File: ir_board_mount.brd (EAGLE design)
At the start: 40 x 51 mm, 15 parts

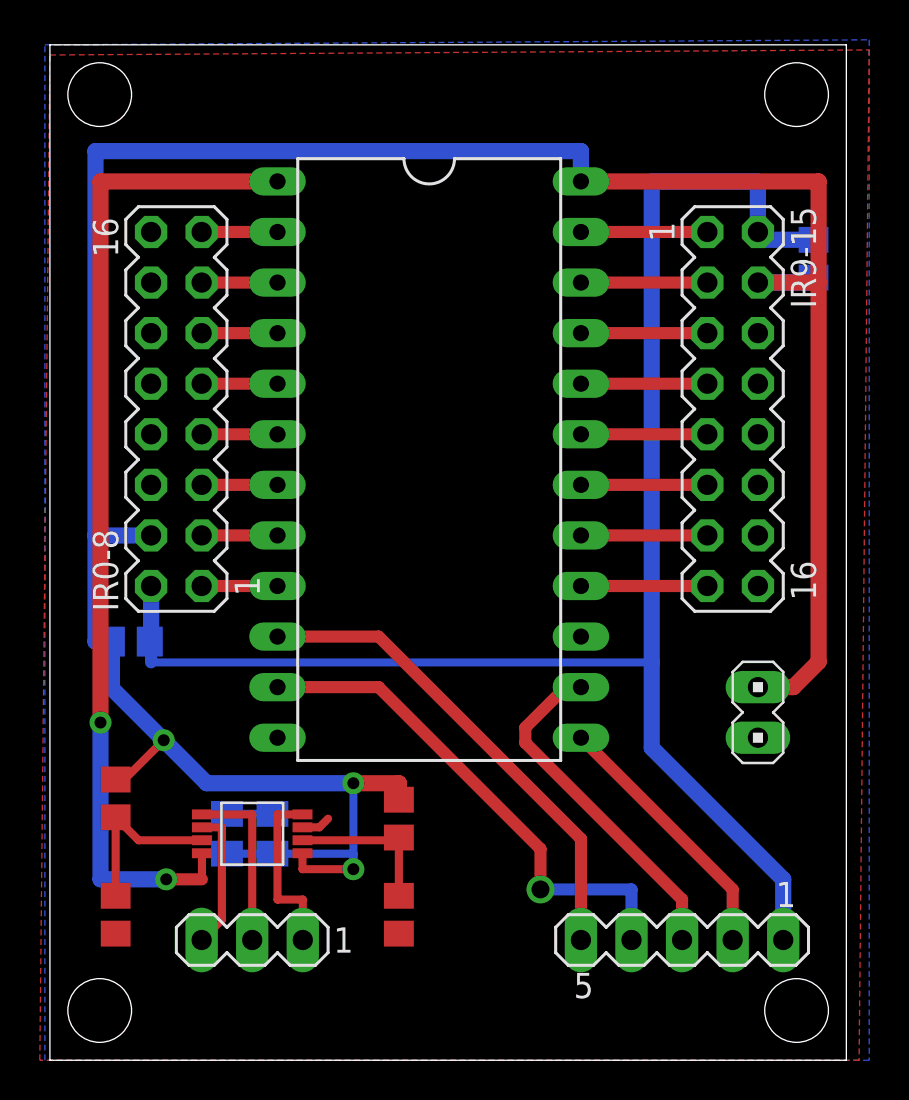
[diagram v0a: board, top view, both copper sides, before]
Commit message: Changed mount holes to vias
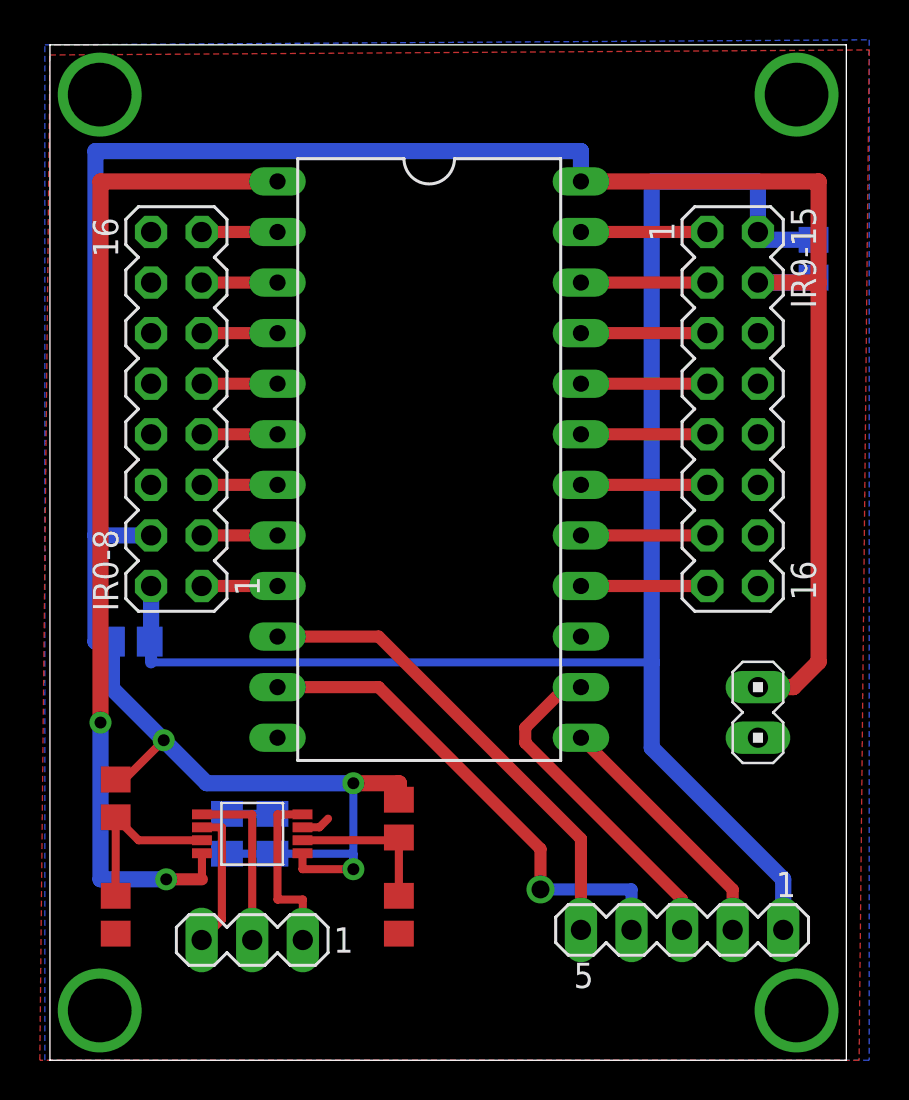
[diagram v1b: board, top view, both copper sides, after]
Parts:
- moved SV5 0.51 mm to (31.8, 3.05)
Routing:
- net N$18: track 17.6 -> 17.1 mm
- net N$17: track 13.3 -> 12.8 mm
- net A: track 24.5 -> 24.0 mm
- net LEDON: track 80.9 -> 80.4 mm
- net B: track 25.7 -> 25.2 mm
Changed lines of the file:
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@@
 v. 2013/11/27</text>
 <text x="14.224" y="9.906" size="0.8128" layer="52" rot="MR0">Debounce Caps</text>
-<hole x="2.5" y="45" drill="3.2"/>
-<hole x="37.5" y="45" drill="3.2"/>
-<hole x="37.5" y="-1" drill="3.2"/>
-<hole x="2.5" y="-1" drill="3.2"/>
 </plain>
 <attributes>
@@
 <attribute name="VALUE" x="18.161" y="38.735" size="1.778" layer="27" ratio="10" rot="R270"/>
 </element>
-<element name="SV5" library="con-lstb" package="MA05-1" value="" x="31.75" y="2.54" smashed="yes" rot="R180">
-<attribute name="OC_NEWARK" value="unknown" x="11.43" y="46.99" size="1.778" layer="27" rot="R180" display="off"/>
-<attribute name="MPN" value="" x="11.43" y="46.99" size="1.778" layer="27" rot="R180" display="off"/>
-<attribute name="MF" value="" x="11.43" y="46.99" size="1.778" layer="27" rot="R180" display="off"/>
-<attribute name="OC_FARNELL" value="unknown" x="11.43" y="46.99" size="1.778" layer="27" rot="R180" display="off"/>
-<attribute name="VALUE" x="34.29" y="5.461" size="1.27" layer="27" ratio="10" rot="R180"/>
+<element name="SV5" library="con-lstb" package="MA05-1" value="" x="31.75" y="3.048" smashed="yes" rot="R180">
+<attribute name="OC_NEWARK" value="unknown" x="11.43" y="47.498" size="1.778" layer="27" rot="R180" display="off"/>
+<attribute name="MPN" value="" x="11.43" y="47.498" size="1.778" layer="27" rot="R180" display="off"/>
+<attribute name="MF" value="" x="11.43" y="47.498" size="1.778" layer="27" rot="R180" display="off"/>
+<attribute name="OC_FARNELL" value="unknown" x="11.43" y="47.498" size="1.778" layer="27" rot="R180" display="off"/>
+<attribute name="VALUE" x="34.29" y="5.969" size="1.27" layer="27" ratio="10" rot="R180"/>
 </element>
 <element name="U$3" library="IEEE_bot_specific_parts" package="TSSOP-8" value="ADC081C021" x="10.16" y="7.874" smashed="yes" rot="R270">
@@
 <contactref element="IR9-15" pad="14"/>
 <contactref element="IR9-15" pad="16"/>
-<polygon width="0.4064" layer="1" isolate="0.254">
+<polygon width="0.4064" layer="1" isolate="0.3048">
 <vertex x="0" y="46.99"/>
 <vertex x="41.148" y="47.244"/>
@@
 <vertex x="-0.508" y="-3.5"/>
 </polygon>
-<polygon width="0.4064" layer="16" isolate="0.254">
+<polygon width="0.4064" layer="16" isolate="0.3048">
 <vertex x="-0.254" y="47.498"/>
 <vertex x="41.148" y="47.752"/>
@@
 <wire x1="5.014" y1="17.526" x2="5.08" y2="17.526" width="0.8128" layer="16"/>
 <wire x1="5.08" y1="17.526" x2="5.08" y2="20.32" width="0.8128" layer="16"/>
-<wire x1="36.83" y1="2.54" x2="36.83" y2="5.588" width="0.8128" layer="16"/>
+<wire x1="36.83" y1="3.048" x2="36.83" y2="5.588" width="0.8128" layer="16"/>
 <wire x1="36.83" y1="5.588" x2="30.226" y2="12.192" width="0.8128" layer="16"/>
 <wire x1="30.226" y1="12.192" x2="30.226" y2="16.4846" width="0.8128" layer="16"/>
@@
 <contactref element="U$2" pad="13"/>
 <contactref element="SV5" pad="2"/>
-<wire x1="34.29" y1="2.54" x2="34.29" y2="5.08" width="0.6096" layer="1"/>
+<wire x1="34.29" y1="3.048" x2="34.29" y2="5.08" width="0.6096" layer="1"/>
 <wire x1="34.29" y1="5.08" x2="26.67" y2="12.7" width="0.6096" layer="1"/>
 </signal>
@@
 <contactref element="SV5" pad="3"/>
 <contactref element="U$2" pad="14"/>
-<wire x1="31.75" y1="2.54" x2="31.75" y2="4.572" width="0.6096" layer="1"/>
+<wire x1="31.75" y1="3.048" x2="31.75" y2="4.572" width="0.6096" layer="1"/>
 <wire x1="31.75" y1="4.572" x2="23.876" y2="12.446" width="0.6096" layer="1"/>
 <wire x1="23.876" y1="12.446" x2="23.876" y2="13.208" width="0.6096" layer="1"/>
@@
 <contactref element="U$2" pad="10"/>
 <contactref element="SV5" pad="5"/>
-<wire x1="26.67" y1="2.54" x2="26.67" y2="7.62" width="0.6096" layer="1"/>
+<wire x1="26.67" y1="3.048" x2="26.67" y2="7.62" width="0.6096" layer="1"/>
 <wire x1="26.67" y1="7.62" x2="16.51" y2="17.78" width="0.6096" layer="1"/>
 <wire x1="16.51" y1="17.78" x2="11.43" y2="17.78" width="0.6096" layer="1"/>
@@
 <contactref element="U$2" pad="11"/>
 <contactref element="SV5" pad="4"/>
-<wire x1="29.21" y1="2.54" x2="29.21" y2="5.08" width="0.6096" layer="16"/>
+<wire x1="29.21" y1="3.048" x2="29.21" y2="5.08" width="0.6096" layer="16"/>
 <wire x1="29.21" y1="5.08" x2="24.638" y2="5.08" width="0.6096" layer="16"/>
 <via x="24.638" y="5.08" extent="1-16" drill="0.9"/>
@@
 <wire x1="4.455" y1="7.549" x2="7.635" y2="7.549" width="0.4064" layer="1"/>
 </signal>
+<signal name="N$20">
+<via x="2.5" y="45" extent="1-16" drill="3.2"/>
+</signal>
+<signal name="N$19">
+<via x="2.5" y="-1" extent="1-16" drill="3.2"/>
+</signal>
+<signal name="N$21">
+<via x="37.5" y="-1" extent="1-16" drill="3.2"/>
+</signal>
+<signal name="N$22">
+<via x="37.5" y="45" extent="1-16" drill="3.2"/>
+</signal>
 </signals>

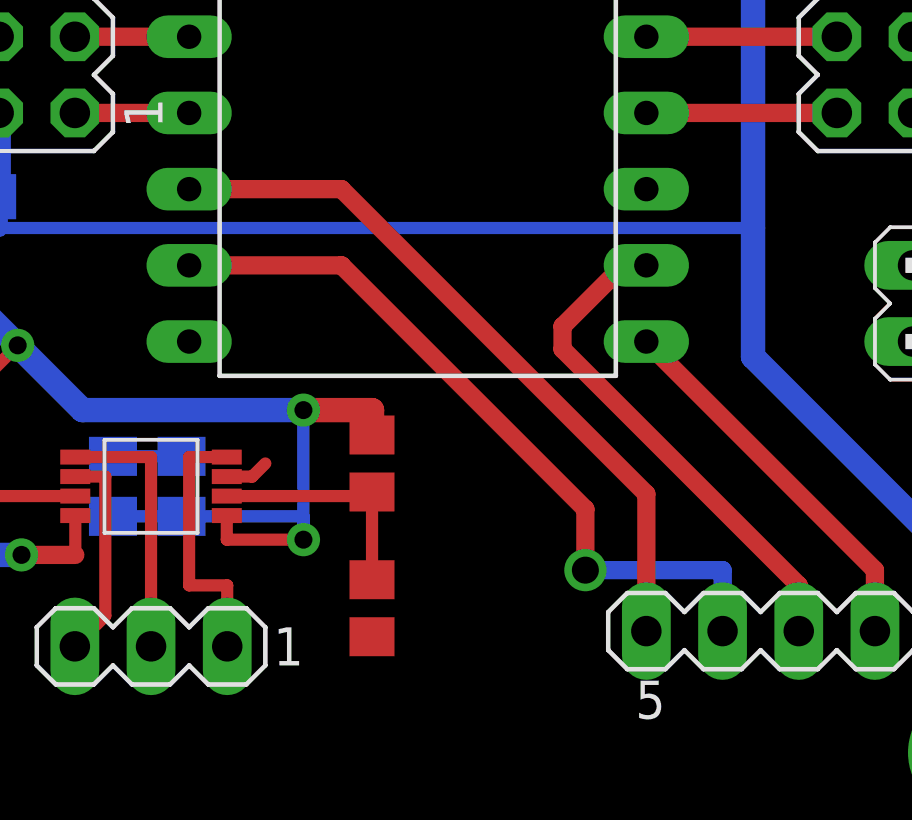
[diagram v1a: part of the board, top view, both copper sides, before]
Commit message: Simplify select line routing and increase clearance
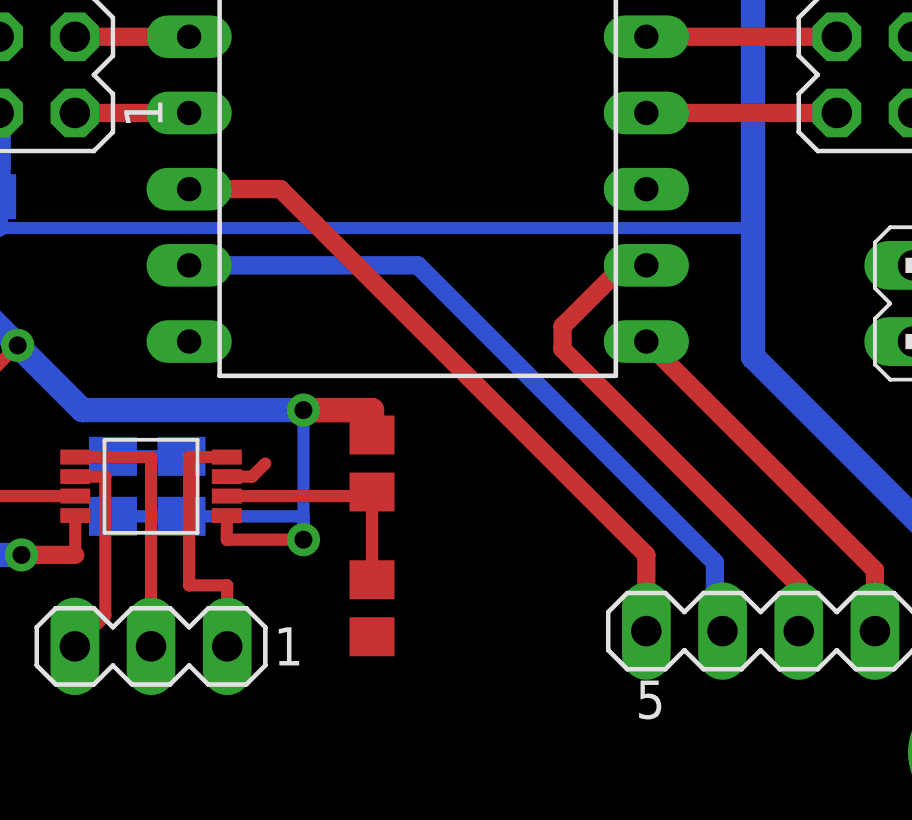
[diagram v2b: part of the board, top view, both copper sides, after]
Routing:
- net A: track 24.0 -> 22.8 mm
- net B: track 25.2 -> 24.0 mm, vias 1 -> 0
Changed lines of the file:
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@@
 <?xml version="1.0" encoding="utf-8"?>
 <!DOCTYPE eagle SYSTEM "eagle.dtd">
-<eagle version="6.5.0">
+<eagle version="6.4">
 <drawing>
 <settings>
@@
 <contactref element="U$2" pad="10"/>
 <contactref element="SV5" pad="5"/>
-<wire x1="26.67" y1="3.048" x2="26.67" y2="7.62" width="0.6096" layer="1"/>
-<wire x1="26.67" y1="7.62" x2="16.51" y2="17.78" width="0.6096" layer="1"/>
-<wire x1="16.51" y1="17.78" x2="11.43" y2="17.78" width="0.6096" layer="1"/>
+<wire x1="26.67" y1="3.048" x2="26.67" y2="5.588" width="0.6096" layer="1"/>
+<wire x1="26.67" y1="5.588" x2="14.478" y2="17.78" width="0.6096" layer="1"/>
+<wire x1="14.478" y1="17.78" x2="11.43" y2="17.78" width="0.6096" layer="1"/>
 </signal>
 <signal name="B">
 <contactref element="U$2" pad="11"/>
 <contactref element="SV5" pad="4"/>
-<wire x1="29.21" y1="3.048" x2="29.21" y2="5.08" width="0.6096" layer="16"/>
-<wire x1="29.21" y1="5.08" x2="24.638" y2="5.08" width="0.6096" layer="16"/>
-<via x="24.638" y="5.08" extent="1-16" drill="0.9"/>
-<wire x1="24.638" y1="5.08" x2="24.638" y2="7.112" width="0.6096" layer="1"/>
-<wire x1="24.638" y1="7.112" x2="16.51" y2="15.24" width="0.6096" layer="1"/>
-<wire x1="16.51" y1="15.24" x2="11.43" y2="15.24" width="0.6096" layer="1"/>
+<wire x1="29.21" y1="3.048" x2="28.956" y2="3.302" width="0.6096" layer="16"/>
+<wire x1="28.956" y1="3.302" x2="28.956" y2="5.334" width="0.6096" layer="16"/>
+<wire x1="28.956" y1="5.334" x2="19.05" y2="15.24" width="0.6096" layer="16"/>
+<wire x1="19.05" y1="15.24" x2="11.43" y2="15.24" width="0.6096" layer="16"/>
 </signal>
 <signal name="OUT">
